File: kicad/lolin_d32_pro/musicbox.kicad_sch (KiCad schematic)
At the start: 16 parts, among them SW1 SW

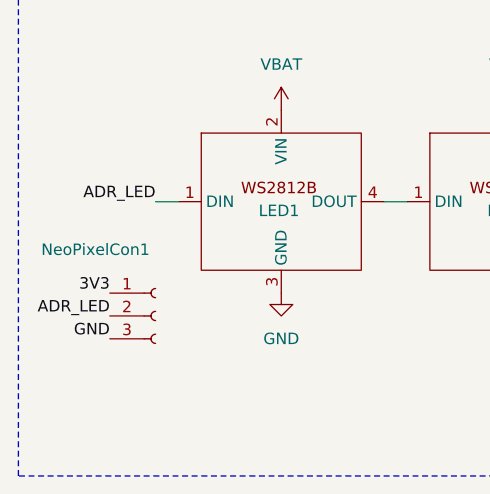
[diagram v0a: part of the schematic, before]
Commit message: Working on Bluetooth Speaker mode
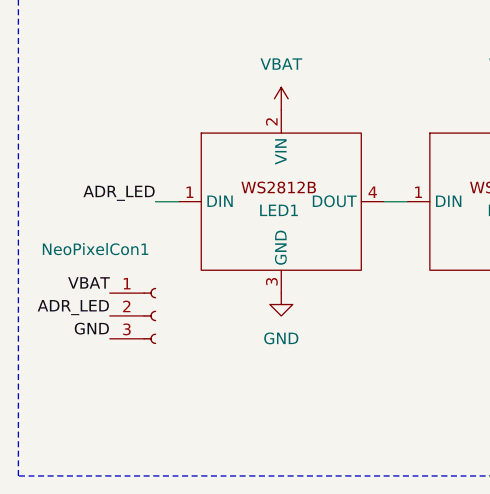
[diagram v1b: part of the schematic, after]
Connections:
- net 3V3: no longer NeoPixelCon1.1 (Pin_1)
- net VBAT: now also NeoPixelCon1.1 (Pin_1)
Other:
- title: ESP32 Musikbox Lolin D32 Pro -> ESP32 Musicbox Lolin D32 Pro
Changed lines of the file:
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@@
 	(paper "A5")
 	(title_block
-		(title "ESP32 Musikbox Lolin D32 Pro")
+		(title "ESP32 Musicbox Lolin D32 Pro")
 		(rev "1.1")
 		(company "Mirko Sertic")
@@
 		)
 	)
-	(label "3V3"
+	(label "VBAT"
 		(at 22.86 114.3 180)
 		(effects
